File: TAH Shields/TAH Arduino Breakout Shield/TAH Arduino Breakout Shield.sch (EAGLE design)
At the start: 7 parts, among them U1 ARDUINOR3-BPLACE

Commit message: TAH Shields new version update
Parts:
- removed U1: ARDUINOR3-BPLACE, Arduino Shield Pin Out:ARDUINOR3-BPLACE
- added M1: ARDUINO_R3_ICSP_NODIM, adafruit:ARDUINO_R3_ICSP_NODIM
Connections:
- new net MISO: M1.MISO, U$1.MISO
- new net MOSI: M1.MOSI, U$1.MOSI
- new net SCK: M1.SCK, U$1.SCK
- net 3.3V: now also M1.3V; no longer U1.3V
- net 5V: now also M1.5V@1, M1.VIN, U$1.ICSP:5V; no longer U1.VIN
- net A0: now also M1.A0; no longer U1.A0
- net A1: now also M1.A1; no longer U1.A1
- net A2: now also M1.A2; no longer U1.A2
- net A3: now also M1.A3; no longer U1.A3
- net A4: now also M1.A4/SDA; no longer U1.A4/SDA
- net A5: now also M1.A5/SCL; no longer U1.A5/SCL
- net D0: now also M1.D0; no longer U1.D0
- net D1: now also M1.D1; no longer U1.D1
- net D10: now also M1.D10; no longer U1.D10
- net D11: now also M1.D11; no longer U1.D11
- net D12: now also M1.D12; no longer U1.D12
- net D13: now also M1.D13; no longer U1.D13
- net D2: now also M1.D2; no longer U1.D2
- net D3: now also M1.D3; no longer U1.D3
- net D4: now also M1.D4; no longer U1.D4
- net D5: now also M1.D5; no longer U1.D5
- net D6: now also M1.D6; no longer U1.D6
- net D7: now also M1.D7; no longer U1.D7
- net D8: now also M1.D8; no longer U1.D8
- net D9: now also M1.D9; no longer U1.D9
- net GND: now also M1.GND, M1.GND@1, M1.GND@2, M1.GND@3; no longer U1.GND, U1.GND1, U1.GND2
- net RESET: now also M1./RESET, M1.RST, U$1.ICSP:RESET; no longer U1./RESET

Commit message: All shields updated with latest Tah footprint
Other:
- moved on the sheet: C1, C2, D3, IC1, U$3

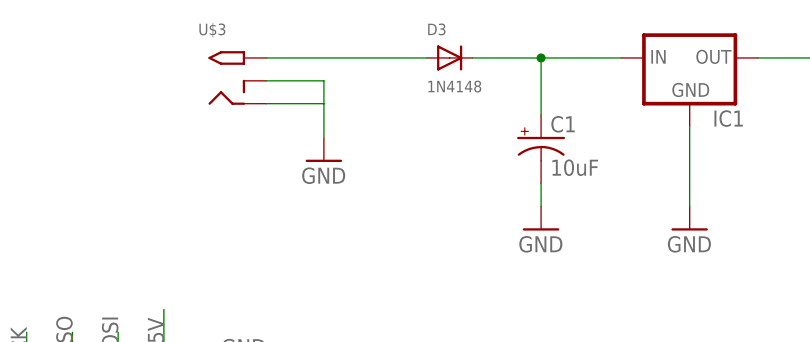
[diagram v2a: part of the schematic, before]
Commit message: Silk Screen related minor changes
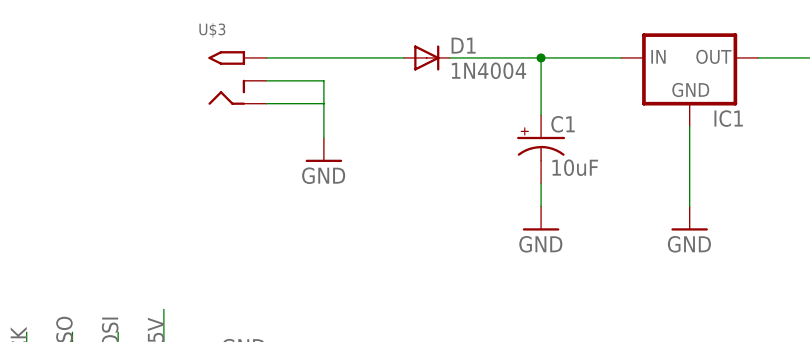
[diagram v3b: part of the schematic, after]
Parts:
- removed D3: 1N4148, 1n4148 diode sot 23:DIODESMA
- added D1: 1N4004, adafruit:1N4004
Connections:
- net N$4: now also D1.A; no longer D3.A
- net N$5: now also D1.C; no longer D3.C
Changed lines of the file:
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@@
 <setting verticaltext="up"/>
 </settings>
-<grid distance="0.1" unitdist="inch" unit="inch" style="lines" multiple="1" display="no" altdistance="0.01" altunitdist="inch" altunit="inch"/>
+<grid distance="0.05" unitdist="inch" unit="inch" style="lines" multiple="1" display="yes" altdistance="0.005" altunitdist="inch" altunit="inch"/>
 <layers>
 <layer number="1" name="Top" color="4" fill="1" visible="no" active="no"/>
@@
 <part name="IC1" library="SparkFun-PowerIC" deviceset="V_REG_78XX" device="-TO-220"/>
 <part name="GND1" library="SparkFun-Aesthetics" deviceset="GND" device=""/>
-<part name="D3" library="1n4148 diode sot 23" deviceset="DIODE" device="SMA" value="1N4148"/>
 <part name="C1" library="Arduino Shield Pin Out" deviceset="CPOL-US" device="E2,5-6E" value="10uF"/>
 <part name="C2" library="Arduino Shield Pin Out" deviceset="CPOL-US" device="E2,5-6E" value="10uF"/>
@@
 <part name="M1" library="adafruit" deviceset="ARDUINO_R3_ICSP" device="_NODIM"/>
 <part name="FRAME1" library="frames" deviceset="A4L-LOC" device=""/>
+<part name="D1" library="adafruit" deviceset="1N4004" device=""/>
 </parts>
 <sheets>
@@
 <instance part="IC1" gate="G$1" x="143.51" y="158.75"/>
 <instance part="GND1" gate="1" x="102.87" y="147.32"/>
-<instance part="D3" gate="G$1" x="116.84" y="158.75"/>
 <instance part="C1" gate="G$1" x="127" y="149.86"/>
 <instance part="C2" gate="G$1" x="161.29" y="149.86"/>
@@
 <instance part="M1" gate="G$1" x="152.4" y="104.14" rot="R270"/>
 <instance part="FRAME1" gate="G$1" x="0" y="0"/>
+<instance part="D1" gate="1" x="114.3" y="158.75"/>
 </instances>
 <busses>
@@
 <segment>
 <pinref part="U$3" gate="G$1" pin="TIP"/>
-<pinref part="D3" gate="G$1" pin="A"/>
-<wire x1="96.52" y1="158.75" x2="114.3" y2="158.75" width="0.1524" layer="91"/>
+<wire x1="96.52" y1="158.75" x2="111.76" y2="158.75" width="0.1524" layer="91"/>
+<pinref part="D1" gate="1" pin="A"/>
 </segment>
 </net>
 <net name="N$5" class="0">
 <segment>
-<pinref part="D3" gate="G$1" pin="C"/>
 <pinref part="IC1" gate="G$1" pin="IN"/>
-<wire x1="119.38" y1="158.75" x2="127" y2="158.75" width="0.1524" layer="91"/>
 <pinref part="C1" gate="G$1" pin="+"/>
 <wire x1="127" y1="158.75" x2="135.89" y2="158.75" width="0.1524" layer="91"/>
 <wire x1="127" y1="152.4" x2="127" y2="158.75" width="0.1524" layer="91"/>
 <junction x="127" y="158.75"/>
-</segment>
-</net>
+<pinref part="D1" gate="1" pin="C"/>
+<wire x1="116.84" y1="158.75" x2="127" y2="158.75" width="0.1524" layer="91"/>
+</segment>
+</net>

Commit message: silk screen related changes
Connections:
- net D2: now also M1.SDA
- net D3: now also M1.SCL
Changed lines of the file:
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@@
 <setting verticaltext="up"/>
 </settings>
-<grid distance="0.05" unitdist="inch" unit="inch" style="lines" multiple="1" display="yes" altdistance="0.005" altunitdist="inch" altunit="inch"/>
+<grid distance="0.1" unitdist="inch" unit="inch" style="lines" multiple="1" display="no" altdistance="0.01" altunitdist="inch" altunit="inch"/>
 <layers>
 <layer number="1" name="Top" color="4" fill="1" visible="no" active="no"/>
@@
 <label x="213.36" y="55.88" size="1.778" layer="95"/>
 </segment>
+<segment>
+<pinref part="M1" gate="G$1" pin="SDA"/>
+<wire x1="208.28" y1="93.98" x2="215.9" y2="93.98" width="0.1524" layer="91"/>
+<label x="213.36" y="93.98" size="1.778" layer="95"/>
+</segment>
 </net>
 <net name="D3" class="0">
@@
 <label x="213.36" y="58.42" size="1.778" layer="95"/>
 </segment>
-</net>
+<segment>
+<pinref part="M1" gate="G$1" pin="SCL"/>
+<wire x1="208.28" y1="96.52" x2="215.9" y2="96.52" width="0.1524" layer="91"/>
+<label x="213.36" y="96.52" size="1.778" layer="95"/>
+</segment>
+</net>
